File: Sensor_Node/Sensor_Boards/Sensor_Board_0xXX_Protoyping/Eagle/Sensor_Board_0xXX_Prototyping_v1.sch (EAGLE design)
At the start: 36 parts, among them J1 M04_SMD_90, J4 ARDUINO_ISP, U2 ATMEGA328P_TQFP, Y1 8MHZ

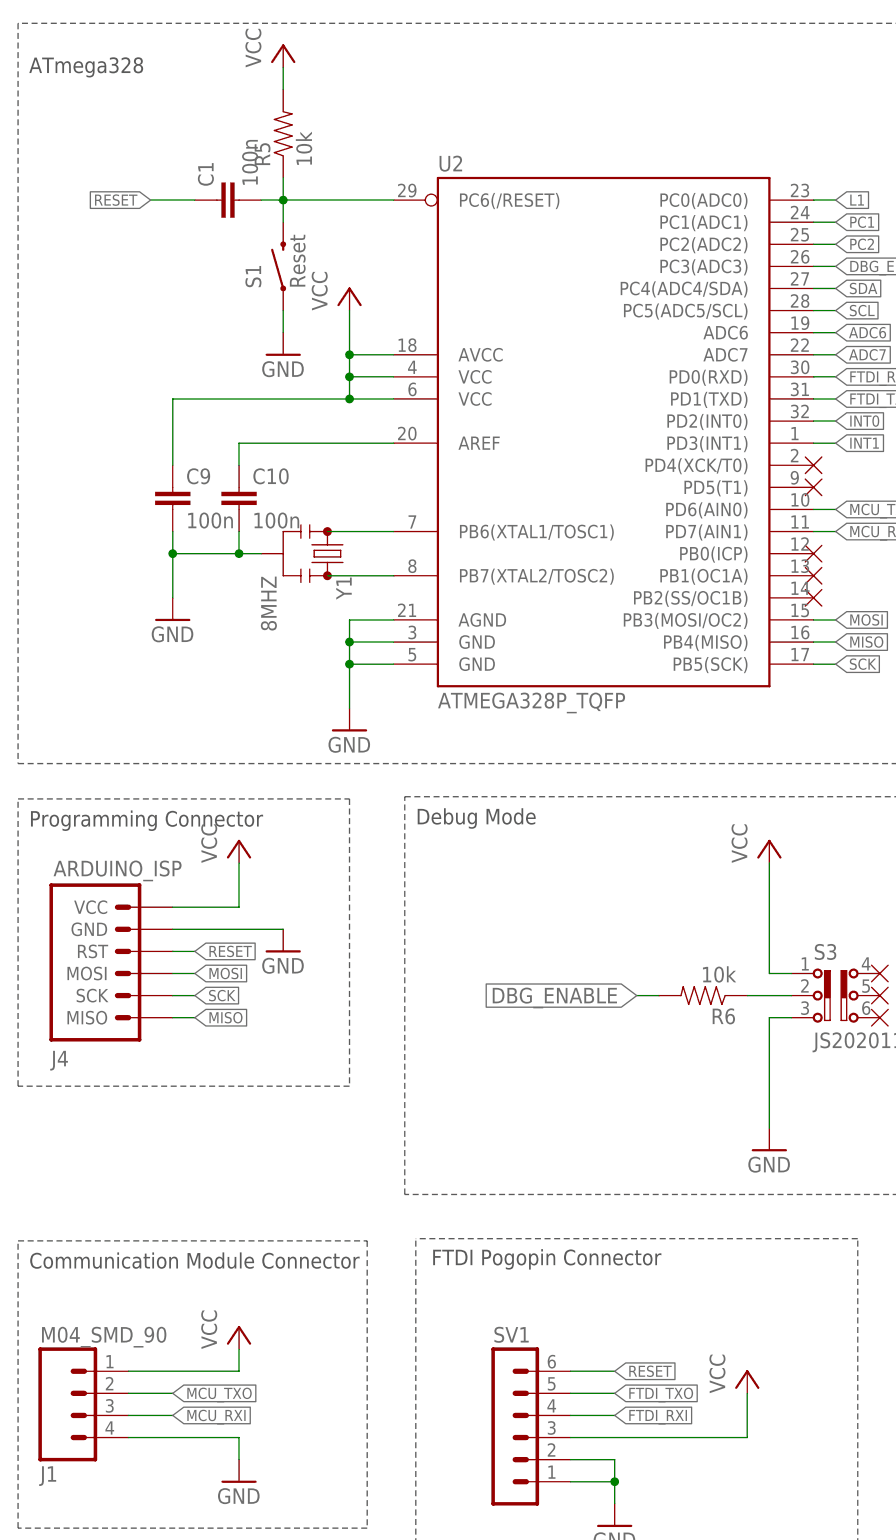
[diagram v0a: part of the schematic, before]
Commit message: Prototype - Board
- reset path
- minor changes
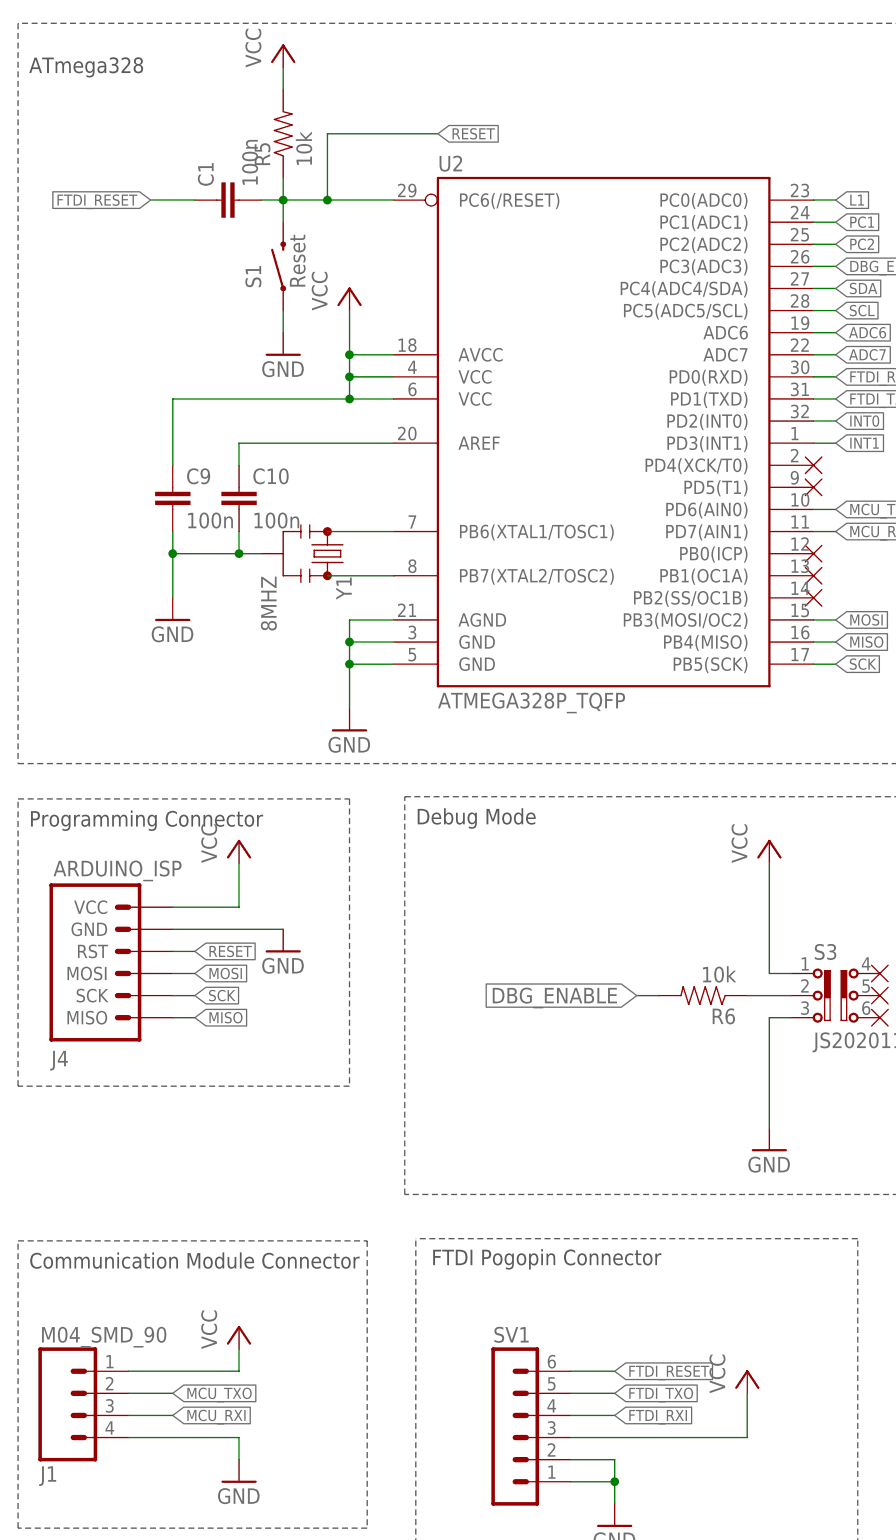
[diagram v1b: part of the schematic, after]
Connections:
- removed net N$4: C1.2, R5.1, S1.RIGHT, U2.PC6(/RESET)
- new net FTDI_RESET: C1.1, SV1.6
- net RESET: now also C1.2, R5.1, S1.RIGHT, U2.PC6(/RESET); no longer C1.1, SV1.6
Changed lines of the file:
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@@
 </segment>
 <segment>
-<label x="22.86" y="182.88" size="1.27" layer="95" rot="R180" xref="yes"/>
-<wire x1="22.86" y1="182.88" x2="27.94" y2="182.88" width="0.1524" layer="91"/>
-<pinref part="C1" gate="G$1" pin="1"/>
-</segment>
-<segment>
-<pinref part="SV1" gate="1" pin="6"/>
-<wire x1="71.12" y1="48.26" x2="76.2" y2="48.26" width="0.1524" layer="91"/>
-<label x="76.2" y="48.26" size="1.27" layer="95" xref="yes"/>
+<pinref part="R5" gate="G$1" pin="1"/>
+<pinref part="S1" gate="G$1" pin="RIGHT"/>
+<wire x1="38.1" y1="185.42" x2="38.1" y2="182.88" width="0.1524" layer="91"/>
+<wire x1="38.1" y1="182.88" x2="38.1" y2="180.34" width="0.1524" layer="91"/>
+<wire x1="35.56" y1="182.88" x2="38.1" y2="182.88" width="0.1524" layer="91"/>
+<junction x="38.1" y="182.88"/>
+<pinref part="U2" gate="U$1" pin="PC6(/RESET)"/>
+<wire x1="38.1" y1="182.88" x2="43.18" y2="182.88" width="0.1524" layer="91"/>
+<pinref part="C1" gate="G$1" pin="2"/>
+<wire x1="43.18" y1="182.88" x2="50.8" y2="182.88" width="0.1524" layer="91"/>
+<wire x1="43.18" y1="182.88" x2="43.18" y2="190.5" width="0.1524" layer="91"/>
+<junction x="43.18" y="182.88"/>
+<wire x1="43.18" y1="190.5" x2="55.88" y2="190.5" width="0.1524" layer="91"/>
+<label x="55.88" y="190.5" size="1.27" layer="95" xref="yes"/>
 </segment>
 </net>
@@
 <pinref part="R6" gate="G$1" pin="1"/>
 <wire x1="96.52" y1="91.44" x2="91.44" y2="91.44" width="0.1524" layer="91"/>
-</segment>
-</net>
-<net name="N$4" class="0">
-<segment>
-<pinref part="R5" gate="G$1" pin="1"/>
-<pinref part="S1" gate="G$1" pin="RIGHT"/>
-<wire x1="38.1" y1="185.42" x2="38.1" y2="182.88" width="0.1524" layer="91"/>
-<wire x1="38.1" y1="182.88" x2="38.1" y2="180.34" width="0.1524" layer="91"/>
-<wire x1="35.56" y1="182.88" x2="38.1" y2="182.88" width="0.1524" layer="91"/>
-<junction x="38.1" y="182.88"/>
-<pinref part="U2" gate="U$1" pin="PC6(/RESET)"/>
-<wire x1="38.1" y1="182.88" x2="50.8" y2="182.88" width="0.1524" layer="91"/>
-<pinref part="C1" gate="G$1" pin="2"/>
 </segment>
 </net>
@@
 </segment>
 </net>
+<net name="FTDI_RESET" class="0">
+<segment>
+<pinref part="SV1" gate="1" pin="6"/>
+<wire x1="71.12" y1="48.26" x2="76.2" y2="48.26" width="0.1524" layer="91"/>
+<label x="76.2" y="48.26" size="1.27" layer="95" xref="yes"/>
+</segment>
+<segment>
+<label x="22.86" y="182.88" size="1.27" layer="95" rot="R180" xref="yes"/>
+<wire x1="22.86" y1="182.88" x2="27.94" y2="182.88" width="0.1524" layer="91"/>
+<pinref part="C1" gate="G$1" pin="1"/>
+</segment>
+</net>

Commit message: Updated Prototyping Board & DS18B20 Board
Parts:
- renumbered C10 to C3, C9 to C2, R5 to R2, R6 to R1, R8 to R3
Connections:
- new net PC0: PAD16.P, PAD7.P, U2.PC0(ADC0)
- net L1: now also U2.PB2(SS/OC1B); no longer PAD16.P, PAD7.P, U2.PC0(ADC0)
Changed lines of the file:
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@@
 <?xml version="1.0" encoding="utf-8"?>
 <!DOCTYPE eagle SYSTEM "eagle.dtd">
-<eagle version="8.2.2">
+<eagle version="8.4.3">
 <drawing>
 <settings>
 <setting alwaysvectorfont="no"/>
+<setting keepoldvectorfont="yes"/>
 <setting verticaltext="up"/>
 </settings>
@@
 <part name="GND16" library="SparkFun" deviceset="GND" device=""/>
 <part name="GND18" library="SparkFun" deviceset="GND" device=""/>
-<part name="R5" library="SparkFun-Passives" deviceset="RESISTOR" device="0805-RES" value="10k"/>
-<part name="C10" library="eagle-ltspice" deviceset="C" device="" value="100n"/>
+<part name="R2" library="SparkFun-Passives" deviceset="RESISTOR" device="0805-RES" value="10k"/>
+<part name="C3" library="eagle-ltspice" deviceset="C" device="" value="100n"/>
 <part name="GND5" library="SparkFun-Aesthetics" deviceset="GND" device=""/>
 <part name="LED1" library="led" deviceset="LED" device="SML0805" value="Red"/>
-<part name="R8" library="SparkFun-Passives" deviceset="RESISTOR" device="0805-RES" value="330"/>
+<part name="R3" library="SparkFun-Passives" deviceset="RESISTOR" device="0805-RES" value="330"/>
 <part name="GND20" library="SparkFun-Aesthetics" deviceset="GND" device=""/>
-<part name="C9" library="eagle-ltspice" deviceset="C" device="" value="100n"/>
-<part name="R6" library="SparkFun-Passives" deviceset="RESISTOR" device="0805-RES" value="10k"/>
+<part name="C2" library="eagle-ltspice" deviceset="C" device="" value="100n"/>
+<part name="R1" library="SparkFun-Passives" deviceset="RESISTOR" device="0805-RES" value="10k"/>
 <part name="GND19" library="SparkFun" deviceset="GND" device=""/>
 <part name="U2" library="marc_library" deviceset="ATMEGA328P_TQFP" device="" value="ATMEGA328P_TQFP"/>
@@
 <part name="U$11" library="myownthings" deviceset="N/C" device=""/>
 <part name="U$12" library="myownthings" deviceset="N/C" device=""/>
-<part name="U$13" library="myownthings" deviceset="N/C" device=""/>
 <part name="U$14" library="myownthings" deviceset="N/C" device=""/>
 <part name="U$15" library="myownthings" deviceset="N/C" device=""/>
@@
 <instance part="GND16" gate="1" x="25.4" y="134.62"/>
 <instance part="GND18" gate="1" x="45.72" y="121.92"/>
-<instance part="R5" gate="G$1" x="38.1" y="190.5" rot="R90"/>
-<instance part="C10" gate="G$1" x="33.02" y="149.86"/>
+<instance part="R2" gate="G$1" x="38.1" y="190.5" rot="R90"/>
+<instance part="C3" gate="G$1" x="33.02" y="149.86"/>
 <instance part="GND5" gate="1" x="38.1" y="96.52"/>
 <instance part="LED1" gate="G$1" x="114.3" y="83.82"/>
-<instance part="R8" gate="G$1" x="114.3" y="96.52" rot="R90"/>
+<instance part="R3" gate="G$1" x="114.3" y="96.52" rot="R90"/>
 <instance part="GND20" gate="1" x="114.3" y="73.66"/>
-<instance part="C9" gate="G$1" x="25.4" y="149.86"/>
-<instance part="R6" gate="G$1" x="86.36" y="91.44" rot="R180"/>
+<instance part="C2" gate="G$1" x="25.4" y="149.86"/>
+<instance part="R1" gate="G$1" x="86.36" y="91.44" rot="R180"/>
 <instance part="GND19" gate="1" x="93.98" y="73.66"/>
 <instance part="U2" gate="U$1" x="55.88" y="127"/>
@@
 <instance part="U$11" gate="G$1" x="99.06" y="142.24"/>
 <instance part="U$12" gate="G$1" x="99.06" y="139.7"/>
-<instance part="U$13" gate="G$1" x="99.06" y="137.16"/>
 <instance part="U$14" gate="G$1" x="106.68" y="93.98"/>
 <instance part="U$15" gate="G$1" x="106.68" y="91.44"/>
@@
 <pinref part="GND16" gate="1" pin="GND"/>
 <wire x1="25.4" y1="137.16" x2="25.4" y2="142.24" width="0.1524" layer="91"/>
-<pinref part="C10" gate="G$1" pin="2"/>
+<pinref part="C3" gate="G$1" pin="2"/>
 <wire x1="33.02" y1="144.78" x2="33.02" y2="142.24" width="0.1524" layer="91"/>
 <junction x="33.02" y="142.24"/>
-<pinref part="C9" gate="G$1" pin="2"/>
+<pinref part="C2" gate="G$1" pin="2"/>
 <wire x1="25.4" y1="142.24" x2="25.4" y2="144.78" width="0.1524" layer="91"/>
 <junction x="25.4" y="142.24"/>
@@
 <wire x1="45.72" y1="160.02" x2="25.4" y2="160.02" width="0.1524" layer="91"/>
 <junction x="45.72" y="160.02"/>
-<pinref part="C9" gate="G$1" pin="1"/>
+<pinref part="C2" gate="G$1" pin="1"/>
 <wire x1="25.4" y1="152.4" x2="25.4" y2="160.02" width="0.1524" layer="91"/>
 <pinref part="P+2" gate="VCC" pin="VCC"/>
@@
 </segment>
 <segment>
-<pinref part="R5" gate="G$1" pin="2"/>
+<pinref part="R2" gate="G$1" pin="2"/>
 <pinref part="P+1" gate="VCC" pin="VCC"/>
 <wire x1="38.1" y1="198.12" x2="38.1" y2="195.58" width="0.1524" layer="91"/>
@@
 </segment>
 <segment>
-<pinref part="R5" gate="G$1" pin="1"/>
+<pinref part="R2" gate="G$1" pin="1"/>
 <pinref part="S1" gate="G$1" pin="RIGHT"/>
 <wire x1="38.1" y1="185.42" x2="38.1" y2="182.88" width="0.1524" layer="91"/>
@@
 <net name="L1" class="0">
 <segment>
-<pinref part="R8" gate="G$1" pin="2"/>
+<pinref part="R3" gate="G$1" pin="2"/>
 <wire x1="114.3" y1="101.6" x2="114.3" y2="106.68" width="0.1524" layer="91"/>
 <label x="114.3" y="106.68" size="1.27" layer="95" rot="R90" xref="yes"/>
 </segment>
 <segment>
-<wire x1="99.06" y1="182.88" x2="101.6" y2="182.88" width="0.1524" layer="91"/>
-<label x="101.6" y="182.88" size="1.27" layer="95" xref="yes"/>
-<pinref part="U2" gate="U$1" pin="PC0(ADC0)"/>
-</segment>
-<segment>
-<wire x1="137.16" y1="132.08" x2="139.7" y2="132.08" width="0.1524" layer="91"/>
-<label x="142.24" y="132.08" size="1.27" layer="95" rot="MR180" xref="yes"/>
-<pinref part="PAD7" gate="1" pin="P"/>
-<pinref part="PAD16" gate="1" pin="P"/>
-<wire x1="139.7" y1="132.08" x2="142.24" y2="132.08" width="0.1524" layer="91"/>
-<wire x1="137.16" y1="127" x2="139.7" y2="127" width="0.1524" layer="91"/>
-<wire x1="139.7" y1="127" x2="139.7" y2="132.08" width="0.1524" layer="91"/>
-<junction x="139.7" y="132.08"/>
+<pinref part="U2" gate="U$1" pin="PB2(SS/OC1B)"/>
+<wire x1="99.06" y1="137.16" x2="101.6" y2="137.16" width="0.1524" layer="91"/>
+<label x="101.6" y="137.16" size="1.27" layer="95" xref="yes"/>
 </segment>
 </net>
@@
 </segment>
 <segment>
-<pinref part="R6" gate="G$1" pin="2"/>
+<pinref part="R1" gate="G$1" pin="2"/>
 <wire x1="81.28" y1="91.44" x2="78.74" y2="91.44" width="0.1524" layer="91"/>
 <label x="78.74" y="91.44" size="1.778" layer="95" rot="R180" xref="yes"/>
@@
 <segment>
 <pinref part="LED1" gate="G$1" pin="A"/>
-<pinref part="R8" gate="G$1" pin="1"/>
+<pinref part="R3" gate="G$1" pin="1"/>
 <wire x1="114.3" y1="86.36" x2="114.3" y2="91.44" width="0.1524" layer="91"/>
 </segment>
@@
 <net name="N$15" class="0">
 <segment>
-<pinref part="C10" gate="G$1" pin="1"/>
+<pinref part="C3" gate="G$1" pin="1"/>
 <pinref part="U2" gate="U$1" pin="AREF"/>
 <wire x1="33.02" y1="152.4" x2="33.02" y2="154.94" width="0.1524" layer="91"/>
@@
 <segment>
 <pinref part="S3" gate="G$1" pin="2"/>
-<pinref part="R6" gate="G$1" pin="1"/>
+<pinref part="R1" gate="G$1" pin="1"/>
 <wire x1="96.52" y1="91.44" x2="91.44" y2="91.44" width="0.1524" layer="91"/>
 </segment>
@@
 </segment>
 </net>
+<net name="PC0" class="0">
+<segment>
+<wire x1="137.16" y1="132.08" x2="139.7" y2="132.08" width="0.1524" layer="91"/>
+<label x="142.24" y="132.08" size="1.27" layer="95" rot="MR180" xref="yes"/>
+<pinref part="PAD7" gate="1" pin="P"/>
+<pinref part="PAD16" gate="1" pin="P"/>
+<wire x1="139.7" y1="132.08" x2="142.24" y2="132.08" width="0.1524" layer="91"/>
+<wire x1="137.16" y1="127" x2="139.7" y2="127" width="0.1524" layer="91"/>
+<wire x1="139.7" y1="127" x2="139.7" y2="132.08" width="0.1524" layer="91"/>
+<junction x="139.7" y="132.08"/>
+</segment>
+<segment>
+<pinref part="U2" gate="U$1" pin="PC0(ADC0)"/>
+<wire x1="99.06" y1="182.88" x2="101.6" y2="182.88" width="0.1524" layer="91"/>
+<label x="101.6" y="182.88" size="1.27" layer="95" xref="yes"/>
+</segment>
+</net>

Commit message: Finished Prototyping Board
- did some tyding up
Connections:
- net GND: now also U$1.P
- net INT0: now also PAD15.P, PAD6.P; no longer PAD14.P, PAD5.P
- net INT1: no longer PAD15.P, PAD6.P
- net VCC: now also PAD14.P, PAD5.P
